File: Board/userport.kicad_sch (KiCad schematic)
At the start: 11 parts, among them P1 PETUSERPORT, U16 LSF0204Q, U17 LSF0204Q, U18 LSF0204Q, U19 LSF0204Q, U23 74LVC1G00

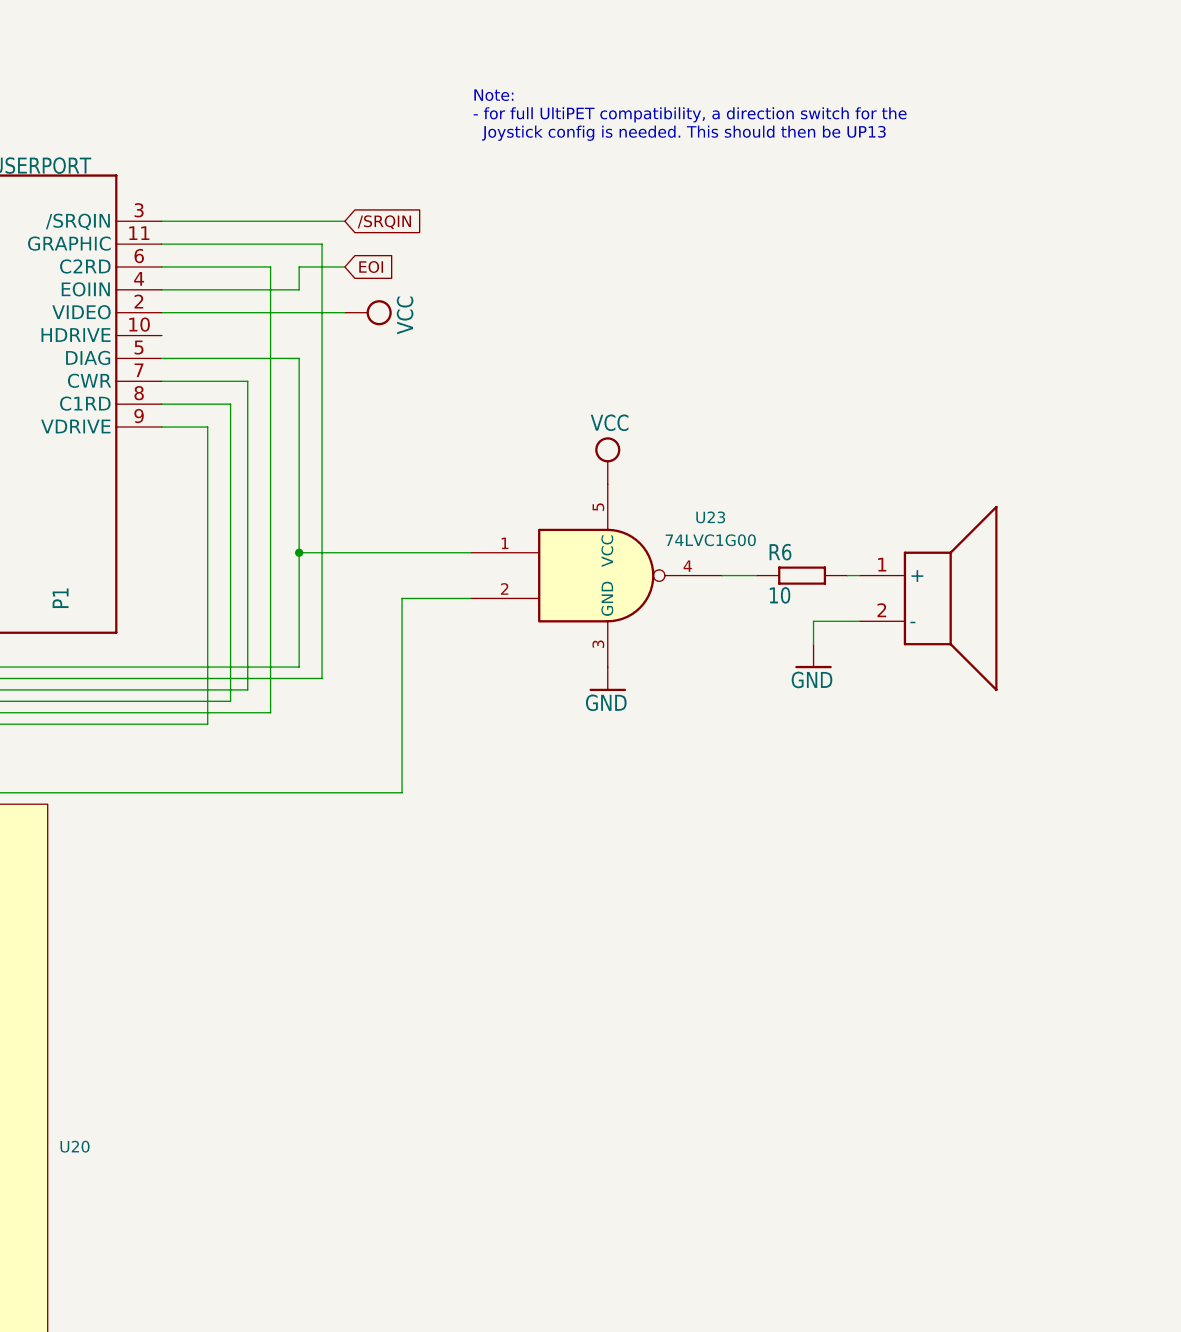
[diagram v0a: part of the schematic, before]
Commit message: added comments and TODOs on schem
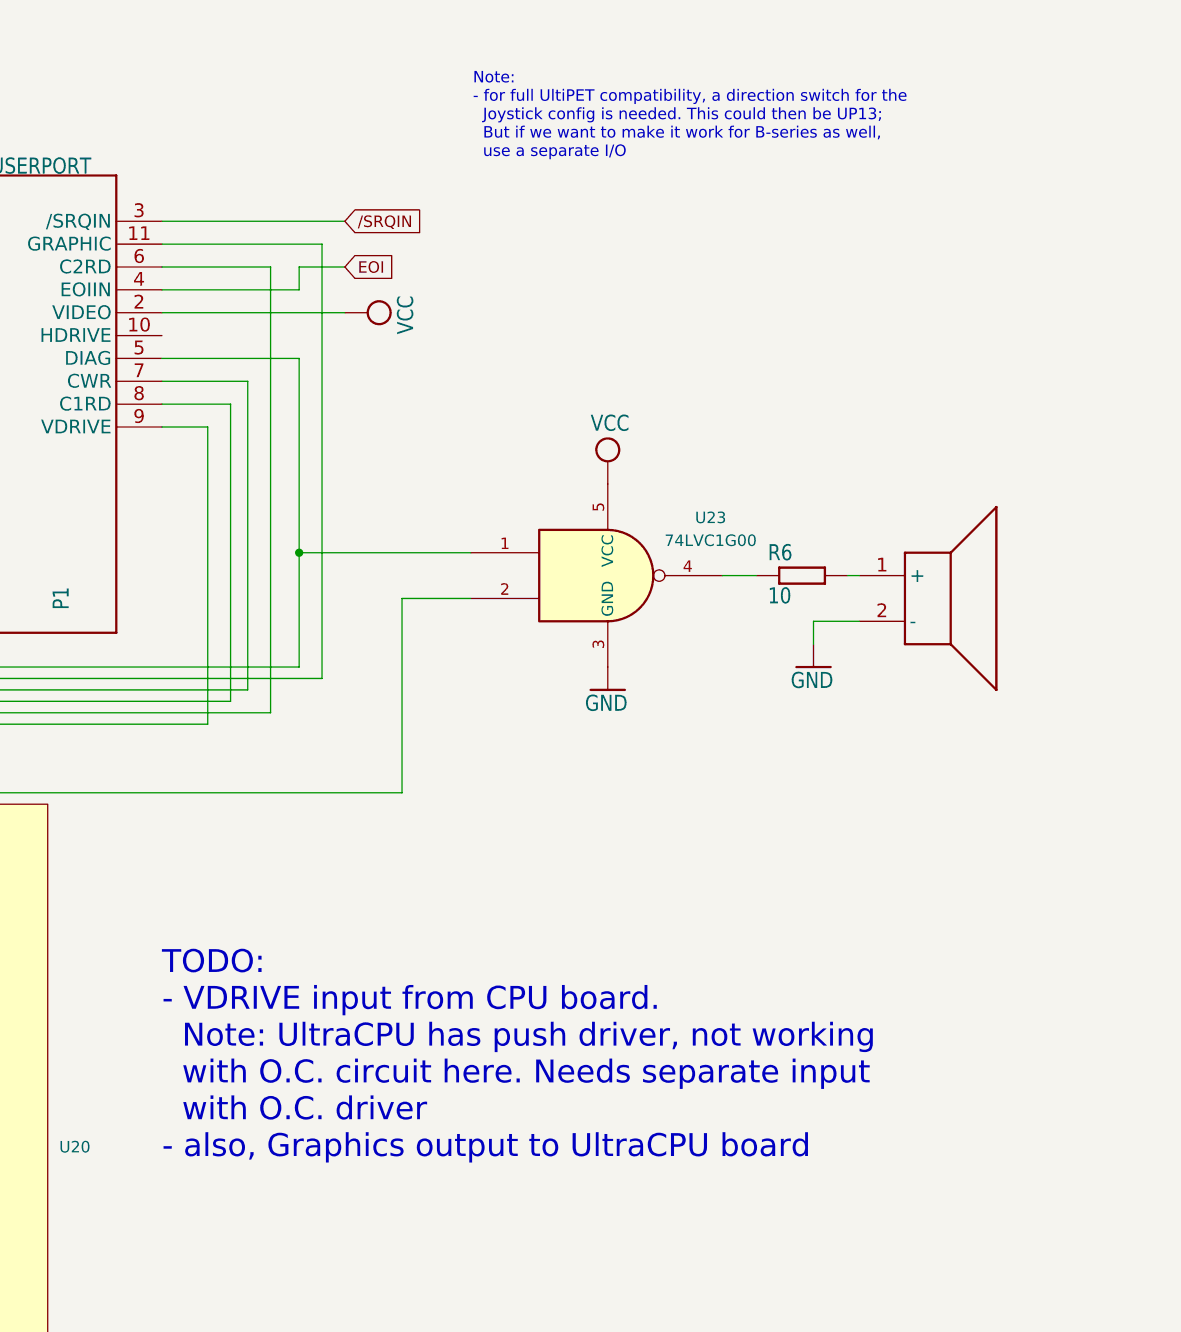
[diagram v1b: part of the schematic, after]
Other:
- note added: "Note: - for full UltiPET compatibility, a direction switch for the Joystick config is needed. This could then be UP13; But if we want to make it work for B-series as well, use a separate I/O"
- note added: "TODO: - VDRIVE input from CPU board. Note: UltraCPU has push driver, not working with O.C. circuit here. Needs separate input with O.C. driver - also, Graphics output to UltraCPU board"
- note removed: "Note: - for full UltiPET compatibility, a direction switch for the Joystick config is needed. This should then be UP13"
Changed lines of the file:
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@@
 	(generator_version "9.0")
 	(paper "A4")
-	(text "Note:\n- for full UltiPET compatibility, a direction switch for the \n  Joystick config is needed. This should then be UP13\n"
+	(text "Note:\n- for full UltiPET compatibility, a direction switch for the \n  Joystick config is needed. This could then be UP13;\n  But if we want to make it work for B-series as well,\n  use a separate I/O\n"
 		(exclude_from_sim no)
 		(at 218.694 26.416 0)
@@
 		)
 	)
+	(text "TODO:\n- VDRIVE input from CPU board. \n  Note: UltraCPU has push driver, not working\n  with O.C. circuit here. Needs separate input\n  with O.C. driver\n- also, Graphics output to UltraCPU board"
+		(exclude_from_sim no)
+		(at 184.15 130.81 0)
+		(effects
+			(font
+				(size 2.54 2.54)
+			)
+			(justify left)
+		)
+	)
 	(text "CSA-CBMIO-V1.0B"
 		(exclude_from_sim no)
@@
 		)
 		(instances
-			(project ""
+			(project "csa_petio_v1"
 				(path "/e52c695d-6540-4a56-9880-06c7d9f215a5/7c8914b4-a2ef-4231-b3f7-1105ec77241e"
 					(reference "U23")
@@
 		)
 		(instances
-			(project ""
+			(project "csa_petio_v1"
 				(path "/e52c695d-6540-4a56-9880-06c7d9f215a5/7c8914b4-a2ef-4231-b3f7-1105ec77241e"
 					(reference "U20")

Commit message: add par ATNA, separate kbd cons, kbd serial input to get more I/O
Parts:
- U20: value ~ -> (none)

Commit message: schem draft done, layout work started
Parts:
- added C147, C150: 0.1u, Capacitor_SMD:C_0805_2012Metric, symbol cbm_ultipet_v1-eagle-import:C-EUC0603
- added D12, D15, D16, D47: 1N4448, Diode_SMD:D_SOD-123, symbol Diode:1N4448
- added J4: Conn_01x02, Connector_PinHeader_2.54mm:PinHeader_1x02_P2.54mm_Horizontal, symbol Connector_Generic:Conn_01x02
- added R10: 4k7, Resistor_SMD:R_0603_1608Metric_Pad0.98x0.95mm_HandSolder, symbol Device:R
- added U14: 74LS06, Package_SO:SO-14_3.9x8.65mm_P1.27mm, symbol 74xx:74LS06
- added U26, U27: CD4053B, Package_SO:SOIC-16_3.9x9.9mm_P1.27mm, symbol Analog_Switch:CD4053B
- added X7, X8: M09-182, Connector_Dsub:DSUB-9_Pins_Vertical_P2.77x2.84mm_MountingHoles, symbol cbm_ultipet_v1-eagle-import:M09-182
- BEEP1: footprint csa_petio_v1:PIEZOBEEPER -> Buzzer_Beeper:MagneticBuzzer_StarMicronics_TMX-H
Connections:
- net GND: now also C147.2, C150.2, U26.6 (INH), U26.7 (VEE), U26.8 (VSS), U27.6 (INH), U27.7 (VEE), U27.8 (VSS), X7.8, X8.8
- net UP4: now also X8.1
- net UP5: now also X8.2
- net UP6: now also X8.3
- net UP7: now also X8.4
- net VCC: now also C147.1, C150.1, R10.1, U26.16 (VDD), U27.16 (VDD), X7.7, X8.7
- net at P1.9 (VDRIVE), RN5.2 (R1), U19.10 (B4)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: now also U14.10
- net at P1.11 (GRAPHIC), RN5.6 (R5), U18.10 (B4)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: now also J4.1 (Pin_1)
- net PUP4: now reaches P1.H (PA4), RN4.5 (R4), U17.10 (B4), U20.7 (2D7)
- net PUP4: now also D15.2 (A)
- net PUP5: now reaches P1.J (PA5), RN4.4 (R3), U17.11 (B3), U20.8 (2D6)
- net PUP5: now also D16.2 (A), U26.13 (A1)
- net PUP6: now reaches P1.K (PA6), RN4.3 (R2), U17.12 (B2), U20.9 (2D5)
- net PUP7: now reaches P1.L (PA7), RN4.2 (R1), U17.13 (B1), U20.10 (2D4)
- net PUP3: now reaches P1.F (PA3), RN4.6 (R5), U16.10 (B4), U20.11 (2D3)
- net PUP3: now also U26.2 (B0), U26.3 (C1)
- net PUP2: now reaches P1.E (PA2), RN4.7 (R6), U16.11 (B3), U20.12 (2D2)
- net PUP2: now also U27.1 (B1), U27.12 (A0)
- net PUP1: now reaches P1.D (PA1), RN4.8 (R7), U16.12 (B2), U20.13 (2D1)
- net PUP1: now also D12.2 (A), U26.1 (B1), U26.5 (C0)
- net PUP0: now reaches P1.C (PA0), RN4.9 (R8), U16.13 (B1), U20.14 (2D0)
- net PUP0: now also D47.2 (A), U27.13 (A1), U27.2 (B0)
- new net: D15.1 (K), D16.1 (K), X8.6
- new net: D12.1 (K), D47.1 (K), U26.12 (A0)
- new net: J4.2 (Pin_2), U14.9
- new net: U26.14 (A), X7.6
- new net: U26.15 (B), X7.4
- new net: U26.4 (C), X7.2
- new net: R10.2, U14.11, U14.8
- new net: U27.14 (A), X7.3
- new net: U27.15 (B), X7.1
- new net OPENHIGH: U27.4 (C)
- new net POTAX: X7.9
- new net POTAY: X7.5
- new net POTBX: X8.9
- new net POTBY: X8.5
- new net UP14: U26.10 (S2), U26.11 (S1), U26.9 (S3), U27.10 (S2), U27.11 (S1), U27.9 (S3)
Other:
- note added: "CSA-CBMIO-V1.1A"
- note added: "CSA-CBMIO-V1.1A-20260824"
- note added: "Double inverter, so default high LS input does not harm if not connected"
- note added: "Down"
- note added: "Fire"
- note added: "GRAPHICS_OUT"
- note added: "High is single Joystick, Low is dual Joystick"
- note added: "Joystick A"
- note added: "Joystick B"
- note added: "Left"
- note added: "Right"
- note added: "Up"
- note added: "V1.1A: - VDRIVE input from CPU board. Note: UltraCPU has push driver, not working with O.C. circuit here. Needs separate input with O.C. driver - also, Graphics output to UltraCPU board - Add joystick switch from UltiPET, but without protection diodes"
- note added: "VSYNC_IN"
- note removed: "CSA-CBMIO-V1.0A-20250815"
- note removed: "CSA-CBMIO-V1.0B"
- note removed: "Note: - for full UltiPET compatibility, a direction switch for the Joystick config is needed. This could then be UP13; But if we want to make it work for B-series as well, use a separate I/O"
- note removed: "TODO: - VDRIVE input from CPU board. Note: UltraCPU has push driver, not working with O.C. circuit here. Needs separate input with O.C. driver - also, Graphics output to UltraCPU board"
- moved on the sheet: P1, R6, RN4, RN5, U16, U17, U18, U19, U20, U23

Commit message: more layout work
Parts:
- added unit 4 of U14
- X7, X8: LCSC (none) -> C189688
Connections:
- net PUP4: now also X8.1
- net PUP5: now also X8.2
- net PUP6: now also X8.3
- net PUP7: now also X8.4
- net UP4: no longer X8.1
- net UP5: no longer X8.2
- net UP6: no longer X8.3
- net UP7: no longer X8.4
- net at J4.2 (Pin_2): now also U14.9; no longer U14.9
- net at R10.2, U14.11: now also U14.8; no longer U14.8
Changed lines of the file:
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@@
 		)
 	)
-	(global_label "UP4"
+	(global_label "PUP4"
 		(shape bidirectional)
 		(at 223.52 67.31 0)
@@
 		)
 		(property "Intersheetrefs" "${INTERSHEET_REFS}"
-			(at 231.268 67.31 0)
+			(at 232.5126 67.31 0)
 			(hide yes)
 			(show_name no)
@@
 		)
 	)
-	(global_label "UP6"
+	(global_label "PUP6"
 		(shape bidirectional)
 		(at 223.52 72.39 0)
@@
 		)
 		(property "Intersheetrefs" "${INTERSHEET_REFS}"
-			(at 231.268 72.39 0)
+			(at 232.5126 72.39 0)
 			(hide yes)
 			(show_name no)
@@
 		)
 	)
-	(global_label "UP7"
+	(global_label "PUP7"
 		(shape bidirectional)
 		(at 223.52 74.93 0)
@@
 		)
 		(property "Intersheetrefs" "${INTERSHEET_REFS}"
-			(at 231.268 74.93 0)
+			(at 232.5126 74.93 0)
 			(hide yes)
 			(show_name no)
@@
 		)
 	)
-	(global_label "UP5"
+	(global_label "PUP5"
 		(shape bidirectional)
 		(at 223.52 69.85 0)
@@
 		)
 		(property "Intersheetrefs" "${INTERSHEET_REFS}"
-			(at 231.268 69.85 0)
+			(at 232.5126 69.85 0)
 			(hide yes)
 			(show_name no)
@@
 			)
 		)
+		(property "LCSC" "C189688"
+			(at 200.66 72.39 0)
+			(hide yes)
+			(show_name no)
+			(do_not_autoplace no)
+			(effects
+				(font
+					(size 1.27 1.27)
+				)
+			)
+		)
 		(pin "2"
 		)
@@
 			(at 283.21 96.52 0)
 			(hide yes)
+			(show_name no)
+			(do_not_autoplace no)
+			(effects
+				(font
+					(size 1.27 1.27)
+				)
+			)
+		)
+		(property "LCSC" "C189688"
+			(at 283.21 96.52 0)
+			(hide yes)

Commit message: cbmio 1.1a draft
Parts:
- C147, C150: value 0.1u -> 100n
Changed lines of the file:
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@@
 			)
 		)
-		(property "Value" "0.1u"
+		(property "Value" "100n"
 			(at 261.874 50.419 0)
 			(show_name no)
@@
 			)
 		)
-		(property "Value" "0.1u"
+		(property "Value" "100n"
 			(at 270.764 50.419 0)
 			(show_name no)
